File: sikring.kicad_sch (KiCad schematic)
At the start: 7 parts, among them IC1 TPS259830LNRGER, IC2 TPS259830LNRGER, IC3 TPS259830LNRGER

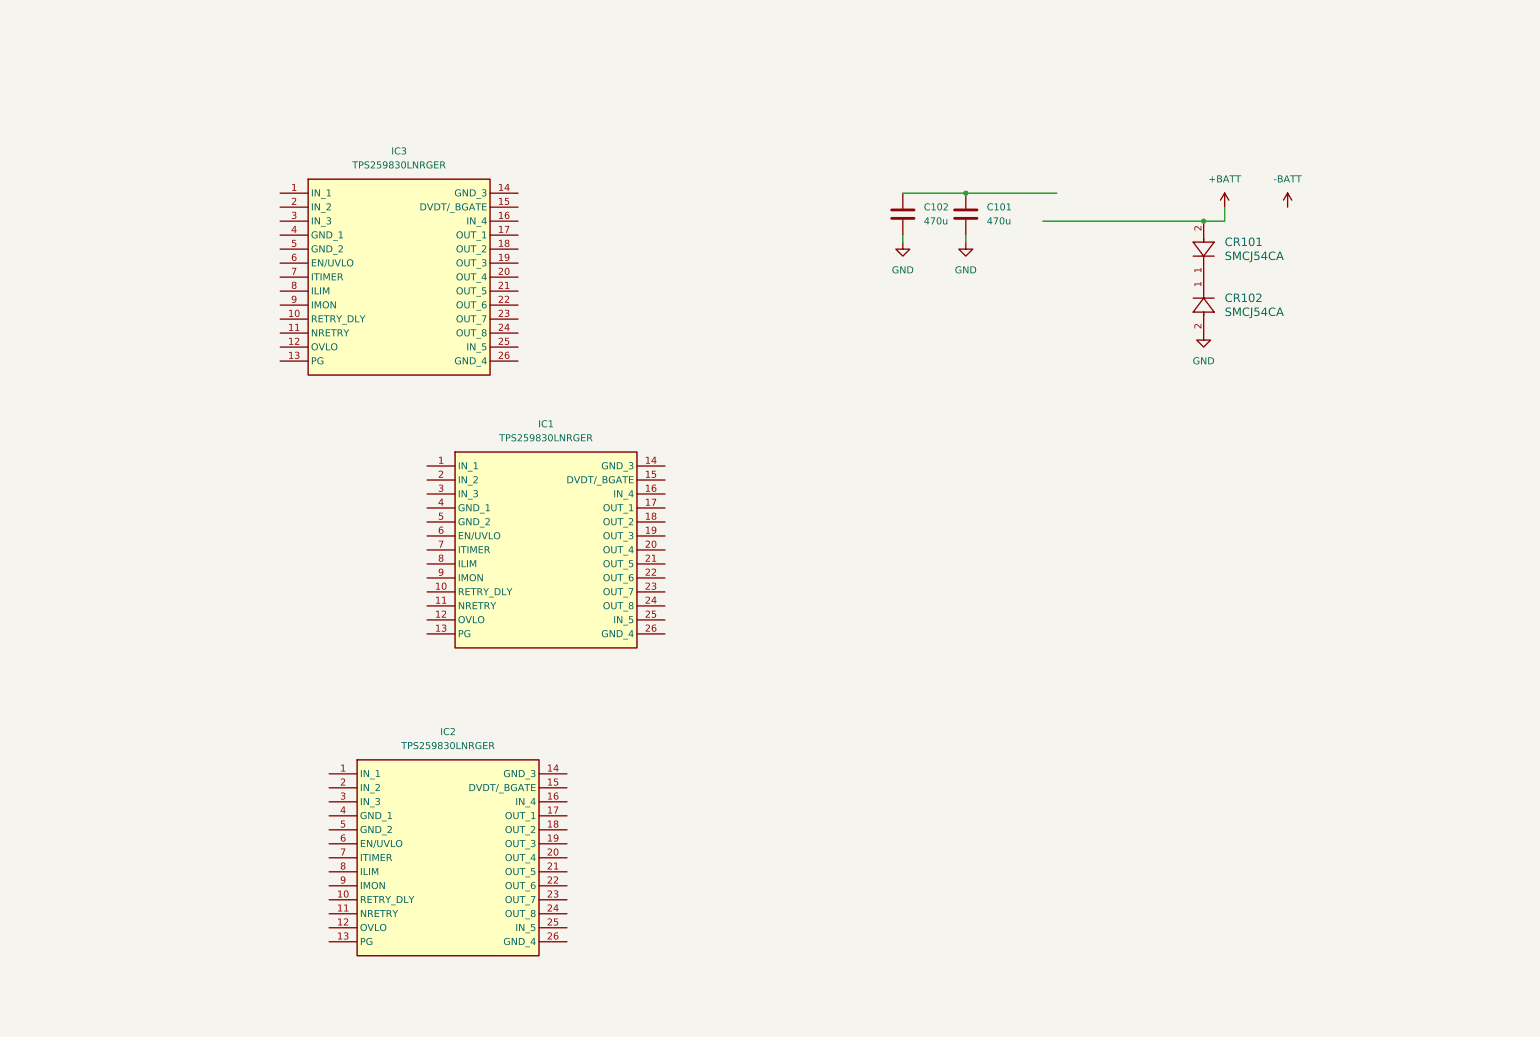
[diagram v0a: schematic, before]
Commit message: lagt til sikring, mangler å plassere dioder
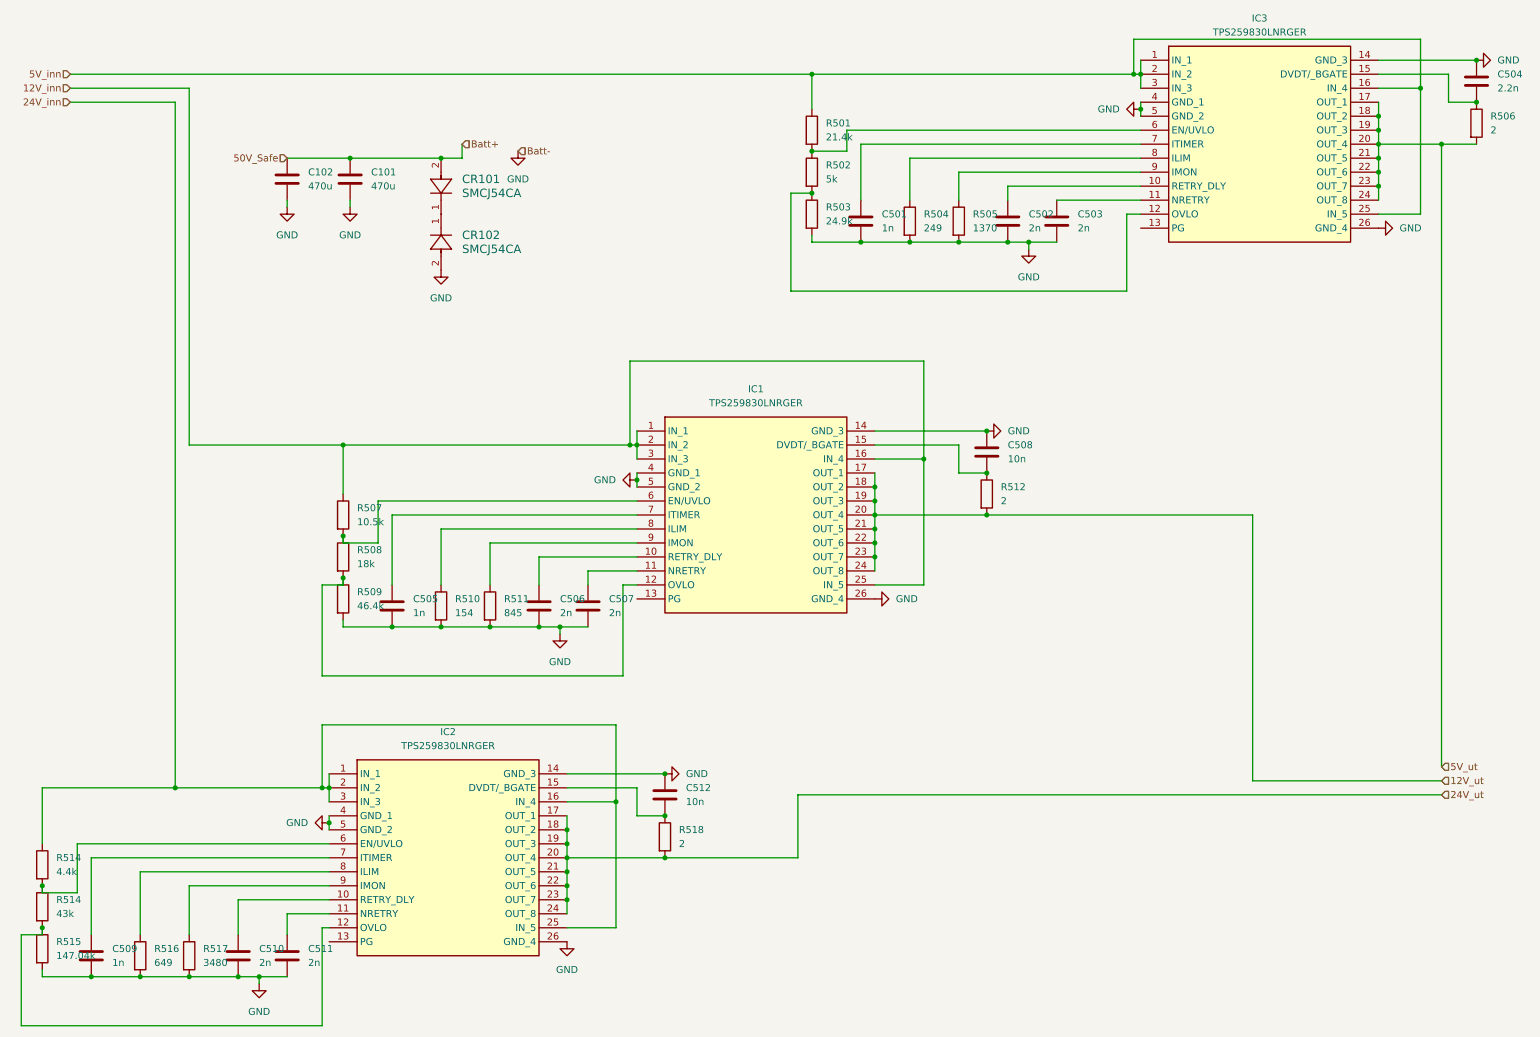
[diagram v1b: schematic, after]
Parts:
- added C501, C505, C509: 1n, symbol Device:C
- added C502, C503, C506, C507, C510, C511: 2n, symbol Device:C
- added C504: 2.2n, symbol Device:C
- added C508, C512: 10n, symbol Device:C
- added R501: 21.4k, CAPAE830X1000N, symbol Device:R
- added R502: 5k, CAPAE830X1000N, symbol Device:R
- added R503: 24.9k, CAPAE830X1000N, symbol Device:R
- added R504: 249, CAPAE830X1000N, symbol Device:R
- added R505: 1370, CAPAE830X1000N, symbol Device:R
- added R506, R512, R518: 2, symbol Device:R
- added R507: 10.5k, CAPAE830X1000N, symbol Device:R
- added R508: 18k, CAPAE830X1000N, symbol Device:R
- added R509: 46.4k, CAPAE830X1000N, symbol Device:R
- added R510: 154, CAPAE830X1000N, symbol Device:R
- added R511: 845, CAPAE830X1000N, symbol Device:R
- added R514: 4.4k, CAPAE830X1000N, symbol Device:R
- added R514: 43k, CAPAE830X1000N, symbol Device:R
- added R515: 147.04k, CAPAE830X1000N, symbol Device:R
- added R516: 649, CAPAE830X1000N, symbol Device:R
- added R517: 3480, CAPAE830X1000N, symbol Device:R
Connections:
- net +BATT is gone; now on net 50V_Safe: CR101.2
- net GND: now also IC1.14 (GND_3), IC1.26 (GND_4), IC1.4 (GND_1), IC1.5 (GND_2), IC2.14 (GND_3), IC2.26 (GND_4), IC2.4 (GND_1), IC2.5 (GND_2), IC3.14 (GND_3), IC3.26 (GND_4), IC3.4 (GND_1), IC3.5 (GND_2), C501.2, C502.2, C503.2, C504.1, C505.2, C506.2, C507.2, C508.1, C509.2, C510.2, C511.2, C512.1, R503.2, R504.2, R505.2, R509.2, R510.2, R511.2, R515.2, R516.2, R517.2
- net 50V_Safe: now reaches C101.2, C102.1
- net 24V_inn: now reaches IC2.1 (IN_1)
- net 24V_inn: now also IC2.16 (IN_4), IC2.2 (IN_2), IC2.25 (IN_5), IC2.3 (IN_3), R514.1
- net at IC2.10 (RETRY_DLY): now also C510.1
- net at IC2.11 (NRETRY): now also C511.1
- net at IC2.12 (OVLO): now also R514.2, R515.1
- net at IC2.15 (DVDT/_BGATE): now also C512.2, R518.1
- net 24V_ut: now reaches IC2.17 (OUT_1)
- net 24V_ut: now also IC2.18 (OUT_2), IC2.19 (OUT_3), IC2.20 (OUT_4), IC2.21 (OUT_5), IC2.22 (OUT_6), IC2.23 (OUT_7), IC2.24 (OUT_8), R518.2
- net at IC2.6 (EN/UVLO): now also R514.1, R514.2
- net at IC2.7 (ITIMER): now also C509.1
- net at IC2.8 (ILIM): now also R516.1
- net at IC2.9 (IMON): now also R517.1
- net 5V_inn: now reaches IC3.1 (IN_1)
- net 5V_inn: now also IC3.16 (IN_4), IC3.2 (IN_2), IC3.25 (IN_5), IC3.3 (IN_3), R501.1
- net at IC3.10 (RETRY_DLY): now also C502.1
- net at IC3.11 (NRETRY): now also C503.1
- net at IC3.12 (OVLO): now also R502.2, R503.1
- net at IC3.15 (DVDT/_BGATE): now also C504.2, R506.1
- net 5V_ut: now reaches IC3.17 (OUT_1)
- net 5V_ut: now also IC3.18 (OUT_2), IC3.19 (OUT_3), IC3.20 (OUT_4), IC3.21 (OUT_5), IC3.22 (OUT_6), IC3.23 (OUT_7), IC3.24 (OUT_8), R506.2
- net at IC3.6 (EN/UVLO): now also R501.2, R502.1
- net at IC3.7 (ITIMER): now also C501.1
- net at IC3.8 (ILIM): now also R504.1
- net at IC3.9 (IMON): now also R505.1
- net 12V_inn: now reaches IC1.1 (IN_1)
- net 12V_inn: now also IC1.16 (IN_4), IC1.2 (IN_2), IC1.25 (IN_5), IC1.3 (IN_3), R507.1
- net at IC1.10 (RETRY_DLY): now also C506.1
- net at IC1.11 (NRETRY): now also C507.1
- net at IC1.12 (OVLO): now also R508.2, R509.1
- net at IC1.15 (DVDT/_BGATE): now also C508.2, R512.1
- net 12V_ut: now reaches IC1.17 (OUT_1)
- net 12V_ut: now also IC1.18 (OUT_2), IC1.19 (OUT_3), IC1.20 (OUT_4), IC1.21 (OUT_5), IC1.22 (OUT_6), IC1.23 (OUT_7), IC1.24 (OUT_8), R512.2
- net at IC1.6 (EN/UVLO): now also R507.2, R508.1
- net at IC1.7 (ITIMER): now also C505.1
- net at IC1.8 (ILIM): now also R510.1
- net at IC1.9 (IMON): now also R511.1
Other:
- moved on the sheet: IC1, IC3
